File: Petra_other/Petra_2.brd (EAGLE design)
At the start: 40.6 x 30.5 mm, 26 parts, among them J2 AVR_SPI_PRG_6NS, J3 Side, J4 Bottom, J5 Top, U1 MIC5219 5V, Y1 16MHz

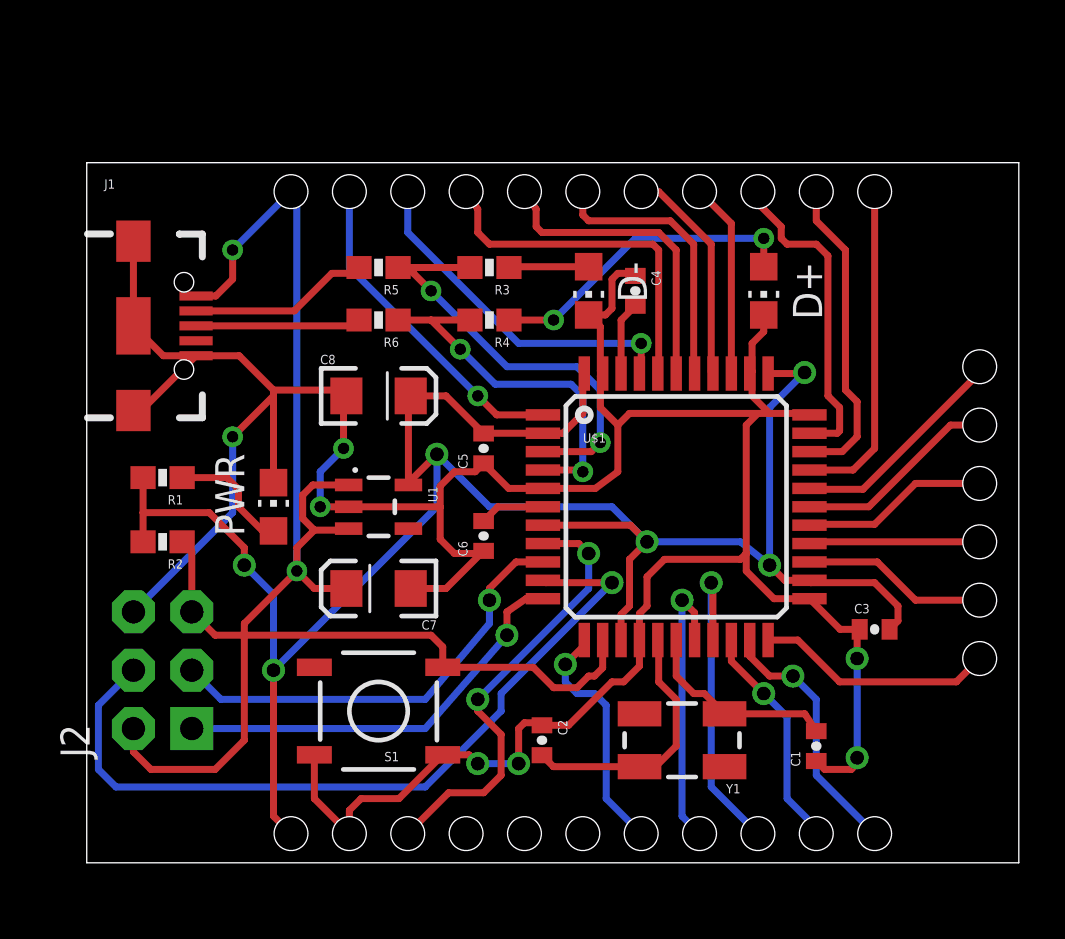
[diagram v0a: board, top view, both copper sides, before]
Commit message: Adding old revisions and  library file.
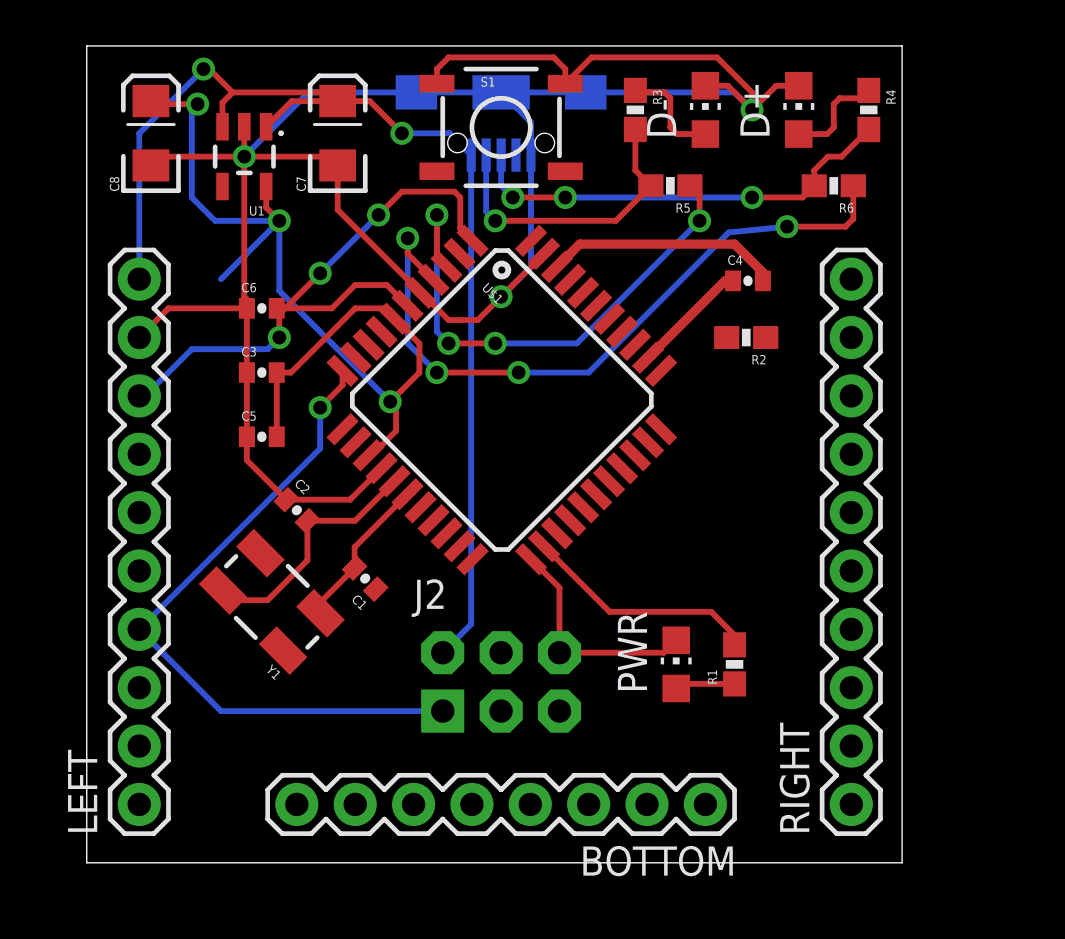
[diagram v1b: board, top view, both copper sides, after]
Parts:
- removed J3: Side, SparkFun-Connectors:1X06_HOLES_ONLY
- removed J4: Bottom, SparkFun-Connectors:1X11_HOLES_ONLY
- removed J5: Top, SparkFun-Connectors:1X11_HOLES_ONLY
- added BOTTOM: (no value), SparkFun-Connectors:1X08_ROUND
- added LEFT, RIGHT: (no value), SparkFun-Connectors:1X10
- moved C3 28.9 mm to (7.62, 21.3)
- moved R2 26.9 mm to (28.7, 22.9)
- moved R1 26.2 mm to (28.2, 8.64), turned to 90 degrees
- moved S1 26.0 mm to (18.0, 32.0), turned to 0 degrees
- moved C1 20.9 mm to (12.1, 12.4), turned to 135 degrees
- moved R6 20.7 mm to (32.5, 29.5)
- moved C7 19.9 mm to (10.9, 31.8), turned to 90 degrees
- moved J1 19.0 mm to (18.0, 33.5), flipped to the bottom, turned to 270 degrees
- moved R4 18.9 mm to (34.0, 32.8), turned to 270 degrees
- moved Y1 18.8 mm to (8.05, 11.4), turned to 135 degrees
- moved PWR 18.8 mm to (25.7, 8.64)
- moved U1 16.3 mm to (6.86, 30.7), turned to 180 degrees
- moved C8 15.1 mm to (2.79, 31.8), turned to 90 degrees
- moved J2 14.7 mm to (18.0, 7.87), turned to 0 degrees
- moved C2 14.6 mm to (9.14, 15.3), turned to 315 degrees
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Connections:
- removed net N$5: J1.D-, R5.2
- removed net N$6: J1.D+, R6.2
- new net A: J1.D-, R3.2, R5.2
- new net B: J1.D+, R4.2, R6.2
- net D+: no longer R4.2
- net D-: no longer R3.2
- net GND: now also LEFT.9; no longer J4.2
- net MISO: now also LEFT.4
- net MOSI: now also LEFT.5
- net PB0: now also LEFT.7; no longer J4.3
- net PB4: now also BOTTOM.2; no longer J3.5
- net PB5: now also BOTTOM.1; no longer J3.6
- net PB6: now also RIGHT.1; no longer J5.11
- net PB7: now also LEFT.3; no longer J4.7
- net PC6: now also RIGHT.2; no longer J5.10
- net PC7: now also RIGHT.3; no longer J5.9
- net PD0: now also LEFT.2; no longer J4.8
- net PD1: now also LEFT.1; no longer J4.9
- net PD4: now also BOTTOM.5; no longer J3.2
- net PD5: now also BOTTOM.6; no longer J3.1
- net PD6: now also BOTTOM.4; no longer J3.3
- net PD7: now also BOTTOM.3; no longer J3.4
- net PE6: now also LEFT.8; no longer J5.2
- net PF0: now also RIGHT.9; no longer J5.3
- net PF1: now also RIGHT.8; no longer J5.4
- net PF4: now also RIGHT.7; no longer J5.5
- net PF5: now also RIGHT.6; no longer J5.6
- net PF6: now also RIGHT.5; no longer J5.7
- net PF7: now also RIGHT.4; no longer J5.8
- net RX: now also BOTTOM.8; no longer J4.10
- net SCK: now also LEFT.6
- net TX: now also BOTTOM.7; no longer J4.11
- net VCC: now also RIGHT.10; no longer J4.1
- net VIN: now also LEFT.10; no longer J5.1
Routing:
- net VCC: track 93.7 -> 52.9 mm, vias 6 -> 3
- net MOSI: track 34.8 -> 0.00 mm, vias 1 -> 0
- net RST: track 24.6 -> 0.00 mm
- net PB0: track 19.4 -> 0.00 mm, vias 2 -> 0
- net SCK: track 19.3 -> 0.00 mm, vias 1 -> 0
- net B: track 0.00 -> 19.2 mm, vias 0 -> 3
- net GND: track 137.5 -> 120.7 mm, vias 7 -> 3
- net PF1: track 15.5 -> 0.00 mm
- net PF0: track 15.3 -> 0.00 mm, vias 1 -> 0
- net D+: track 16.2 -> 30.9 mm, vias 2 -> 4
- net PB6: track 14.4 -> 0.00 mm
- net PD1: track 14.3 -> 0.00 mm, vias 1 -> 0
- net PC7: track 14.0 -> 0.00 mm
- net PC6: track 13.7 -> 0.00 mm
- net PF4: track 13.6 -> 0.00 mm
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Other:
- board size 40.6 x 30.5 mm -> 35.5 x 35.5 mm
